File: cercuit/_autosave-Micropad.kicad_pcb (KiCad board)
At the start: 2 copper layers, 24 parts, among them SW1 SW_Push, SW10 SW_Push, SW11 SW_Push, SW12 SW_Push, SW2 SW_Push, SW3 SW_Push, SW4 SW_Push, SW5 SW_Push, SW6 SW_Push, SW7 SW_Push, SW8 SW_Push, SW9 SW_Push

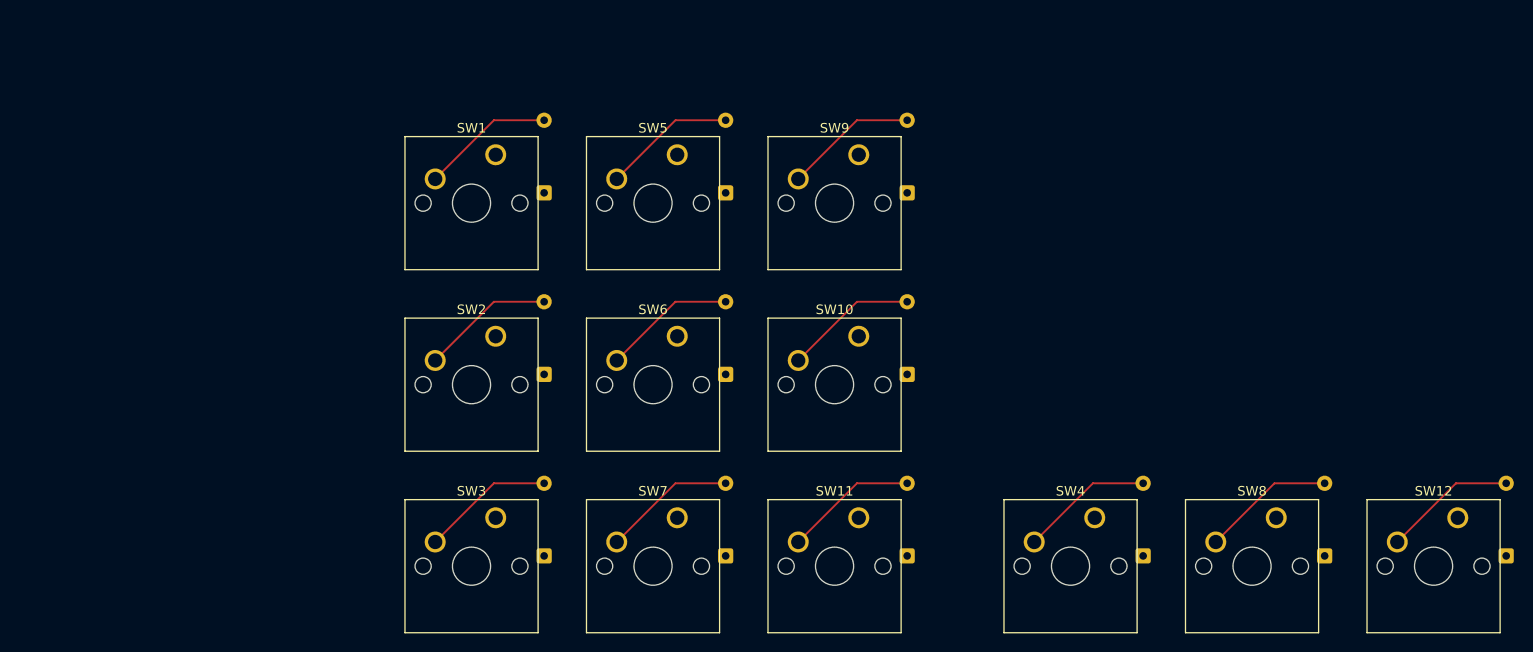
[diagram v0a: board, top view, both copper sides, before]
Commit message: updated the shchmatics swich placenmet and connected the pcb switch and diode
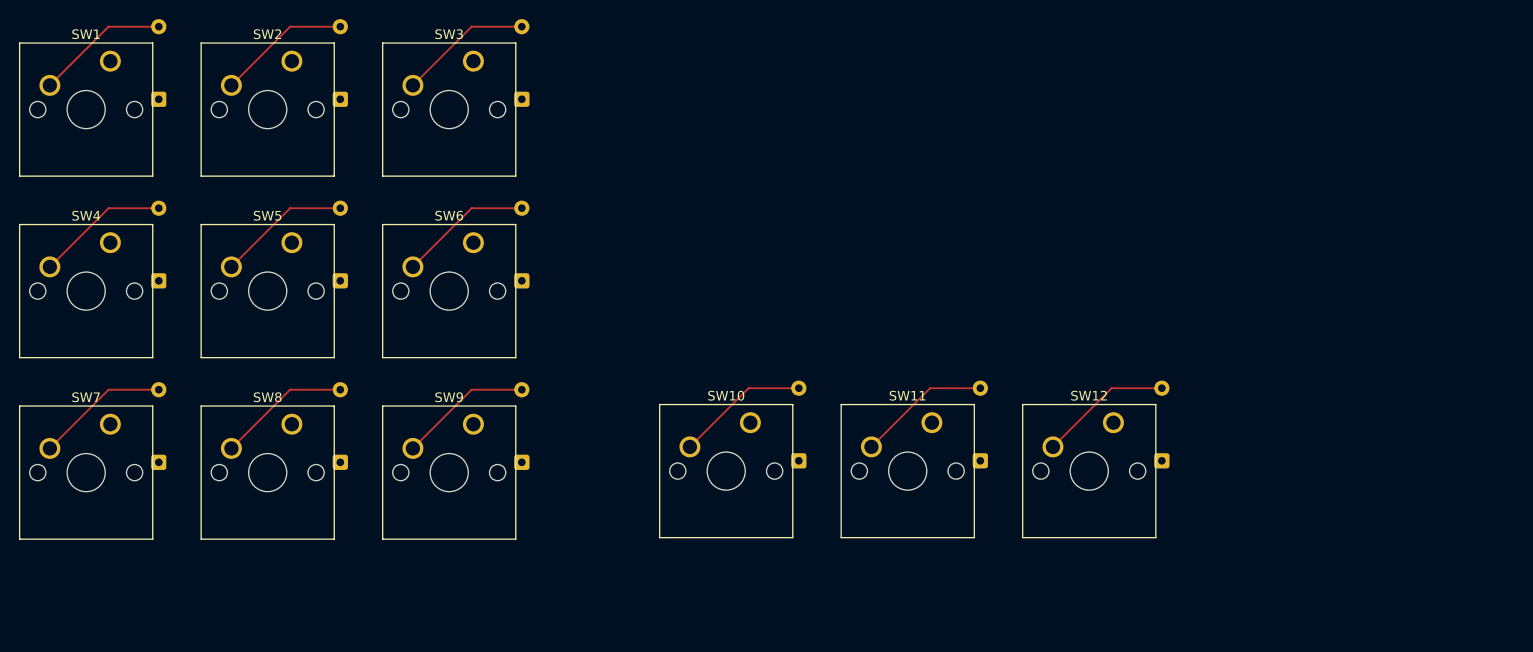
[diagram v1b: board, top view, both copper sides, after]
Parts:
- moved SW4 107.3 mm to (38.1, 57.1)
- moved SW8 103.8 mm to (57.1, 76.2)
- moved SW7 60.3 mm to (38.1, 76.2)
- moved SW9 49.3 mm to (76.2, 76.2)
- moved SW3 48.0 mm to (76.2, 38.1)
- moved D1 41.6 mm to (43.2, 42.1)
- moved D2 41.6 mm to (62.2, 42.1)
- moved D4 41.6 mm to (43.2, 61.1)
- moved D5 41.6 mm to (62.2, 61.1)
- moved D7 41.6 mm to (43.2, 80.2)
- moved D8 41.6 mm to (62.2, 80.2)
- moved SW1 41.6 mm to (38.1, 38.1)
- moved D3 41.6 mm to (81.3, 42.1)
- moved D6 41.6 mm to (81.3, 61.1)
- moved D9 41.6 mm to (81.3, 80.2)
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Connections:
- D10 pad 1: /Row 1 -> /Row 3
- D11 pad 1: /Row 2 -> /Row 3
- D2 pad 1: /Row 1 -> /Row 0
- D3 pad 1: /Row 2 -> /Row 0
- D4 pad 1: /Row 3 -> /Row 1
- D5 pad 1: /Row 0 -> /Row 1
- D8 pad 1: /Row 3 -> /Row 2
- D9 pad 1: /Row 0 -> /Row 2
- SW10 pad 1: /col 1 -> /col 0
- SW10 pad 2: Net-(D6-A) -> Net-(D10-A)
- SW11 pad 1: /col 2 -> /col 1
- SW11 pad 2: Net-(D9-A) -> Net-(D11-A)
- SW2 pad 1: /col 0 -> /col 1
- SW2 pad 2: Net-(D4-A) -> Net-(D2-A)
- SW3 pad 1: /col 1 -> /col 2
- SW3 pad 2: Net-(D7-A) -> Net-(D3-A)
- SW4 pad 1: /col 2 -> /col 0
- SW4 pad 2: Net-(D10-A) -> Net-(D4-A)
- SW5 pad 1: /col 0 -> /col 1
- SW5 pad 2: Net-(D2-A) -> Net-(D5-A)
- SW6 pad 1: /col 1 -> /col 2
- SW6 pad 2: Net-(D5-A) -> Net-(D6-A)
- SW7 pad 1: /col 1 -> /col 0
- SW7 pad 2: Net-(D8-A) -> Net-(D7-A)
- SW8 pad 1: /col 2 -> /col 1
- SW8 pad 2: Net-(D11-A) -> Net-(D8-A)
- SW9 pad 1: /col 0 -> /col 2
- SW9 pad 2: Net-(D3-A) -> Net-(D9-A)
